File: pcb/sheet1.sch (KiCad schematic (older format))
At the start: 316 parts, among them J16 Aud_Conn, J17 Main_Connector, J18 Cat_Box_Conn, J20 J20, Q1 2N3904, Q3 Q_NPN_BCE, Q4 Q_NPN_BCE, SW1 L_11, SW2 D_10, SW3 E/F_10, Y1 12.096MHz

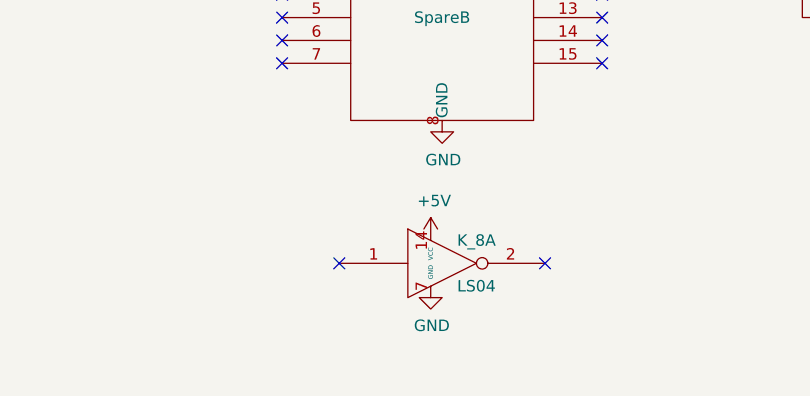
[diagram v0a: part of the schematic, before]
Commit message: Added more power traces
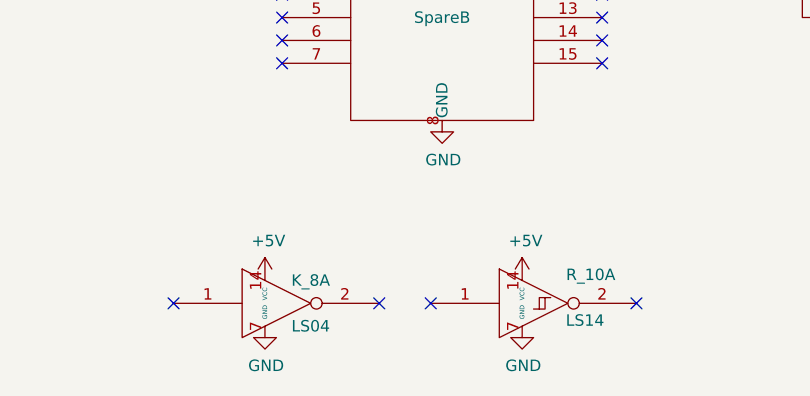
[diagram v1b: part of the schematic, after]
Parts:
- added unit 1 of R_10
- C69, R11: footprint (none) -> Star_Wars_Vector_PCB:GenericComp
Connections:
- net +5V: now also R_10.14 (VCC)
- net GND: now also R_10.7 (GND)
- no-connect marks 180 -> 182
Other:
- moved on the sheet: K_8A
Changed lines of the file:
@@
 F 0 "C69" H 1815 5196 50  0000 L CNN
 F 1 ".1uf" H 1815 5105 50  0000 L CNN
-F 2 "" H 1738 5000 50  0001 C CNN
+F 2 "Star_Wars_Vector_PCB:GenericComp" H 1738 5000 50  0001 C CNN
 F 3 "~" H 1700 5150 50  0001 C CNN
 	1    1700 5150
@@
 F 0 "R11" V 12825 6400 50  0000 C CNN
 F 1 "10k" V 12675 6400 50  0000 C CNN
-F 2 "" V 12790 6390 50  0001 C CNN
+F 2 "Star_Wars_Vector_PCB:GenericComp" V 12790 6390 50  0001 C CNN
 F 3 "~" H 12750 6400 50  0001 C CNN
 	1    12750 6400
@@
 L Asteroids:LS04 K_8
 U 1 1 656FCECD
-P 40425 32050
-F 0 "K_8" H 40575 32150 50  0000 C CNN
-F 1 "LS04" H 40575 31950 50  0000 C CNN
-F 2 "Star_Wars_Vector_PCB:DIP14" H 40425 32050 50  0001 C CNN
-F 3 "" H 40425 32050 50  0001 C CNN
-	1    40425 32050
+P 39700 32225
+F 0 "K_8" H 39850 32325 50  0000 C CNN
+F 1 "LS04" H 39850 32125 50  0000 C CNN
+F 2 "Star_Wars_Vector_PCB:DIP14" H 39700 32225 50  0001 C CNN
+F 3 "" H 39700 32225 50  0001 C CNN
+	1    39700 32225
 	1    0    0    -1
 $EndComp
@@
 L power:GND #PWR0509
 U 1 1 6570845A
-P 40375 32150
-F 0 "#PWR0509" H 40375 31900 50  0001 C CNN
-F 1 "GND" H 40380 31977 50  0000 C CNN
-F 2 "" H 40375 32150 50  0001 C CNN
-F 3 "" H 40375 32150 50  0001 C CNN
-	1    40375 32150
+P 39650 32325
+F 0 "#PWR0509" H 39650 32075 50  0001 C CNN
+F 1 "GND" H 39655 32152 50  0000 C CNN
+F 2 "" H 39650 32325 50  0001 C CNN
+F 3 "" H 39650 32325 50  0001 C CNN
+	1    39650 32325
 	1    0    0    -1
 $EndComp
@@
 L power:+5V #PWR0510
 U 1 1 6570E245
-P 40375 31950
-F 0 "#PWR0510" H 40375 31800 50  0001 C CNN
-F 1 "+5V" H 40390 32123 50  0000 C CNN
-F 2 "" H 40375 31950 50  0001 C CNN
-F 3 "" H 40375 31950 50  0001 C CNN
-	1    40375 31950
+P 39650 32125
+F 0 "#PWR0510" H 39650 31975 50  0001 C CNN
+F 1 "+5V" H 39665 32298 50  0000 C CNN
+F 2 "" H 39650 32125 50  0001 C CNN
+F 3 "" H 39650 32125 50  0001 C CNN
+	1    39650 32125
 	1    0    0    -1
 $EndComp
-NoConn ~ 40875 32050
-NoConn ~ 39975 32050
+NoConn ~ 40150 32225
+NoConn ~ 39250 32225
 NoConn ~ 45200 30250
 NoConn ~ 43950 30350
@@
 	45450 30800 45725 30800
 Connection ~ 45725 30800
+$Comp
+L Star_Wars_Vector_PCB:LS14 R_10
+U 1 1 61140B43
+P 40825 32225
+F 0 "R_10" H 41075 32350 50  0000 C CNN
+F 1 "LS14" H 41050 32150 50  0000 C CNN
+F 2 "" H 40925 32225 50  0001 C CNN
+F 3 "" H 40925 32225 50  0001 C CNN
+	1    40825 32225
+	1    0    0    -1
+$EndComp
+NoConn ~ 41275 32225
+NoConn ~ 40375 32225
+$Comp
+L power:+5V #PWR?
+U 1 1 6193CE8D
+P 40775 32125
+F 0 "#PWR?" H 40775 31975 50  0001 C CNN
+F 1 "+5V" H 40790 32298 50  0000 C CNN
+F 2 "" H 40775 32125 50  0001 C CNN
+F 3 "" H 40775 32125 50  0001 C CNN
+	1    40775 32125
+	1    0    0    -1
+$EndComp
+$Comp
+L power:GND #PWR?
+U 1 1 6194245E
+P 40775 32325
+F 0 "#PWR?" H 40775 32075 50  0001 C CNN
+F 1 "GND" H 40780 32152 50  0000 C CNN
+F 2 "" H 40775 32325 50  0001 C CNN
+F 3 "" H 40775 32325 50  0001 C CNN
+	1    40775 32325
+	1    0    0    -1
+$EndComp
 $EndSCHEMATC

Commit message: Finished the power traces
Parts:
- C81: footprint (none) -> Star_Wars_Vector_PCB:GenericComp
- C93, C94: footprint (none) -> Star_Wars_Main_PCB:Cap1
- R_10: footprint (none) -> Star_Wars_Vector_PCB:DIP14
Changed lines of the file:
@@
 F 0 "C81" H 2665 5921 50  0000 L CNN
 F 1 ".1uf" H 2665 5830 50  0000 L CNN
-F 2 "" H 2588 5725 50  0001 C CNN
+F 2 "Star_Wars_Vector_PCB:GenericComp" H 2588 5725 50  0001 C CNN
 F 3 "~" H 2550 5875 50  0001 C CNN
 	1    2550 5875
@@
 F 0 "C93" H 3640 7996 50  0000 L CNN
 F 1 "10uf 25V" H 3640 7905 50  0000 L CNN
-F 2 "" H 3525 7950 50  0001 C CNN
+F 2 "Star_Wars_Main_PCB:Cap1" H 3525 7950 50  0001 C CNN
 F 3 "~" H 3525 7950 50  0001 C CNN
 	1    3525 7950
@@
 F 0 "C94" H 33090 2046 50  0000 L CNN
 F 1 "4.7uf" H 33090 1955 50  0000 L CNN
-F 2 "" H 32975 2000 50  0001 C CNN
+F 2 "Star_Wars_Main_PCB:Cap1" H 32975 2000 50  0001 C CNN
 F 3 "~" H 32975 2000 50  0001 C CNN
 	1    32975 2000
@@
 F 0 "R_10" H 41075 32350 50  0000 C CNN
 F 1 "LS14" H 41050 32150 50  0000 C CNN
-F 2 "" H 40925 32225 50  0001 C CNN
+F 2 "Star_Wars_Vector_PCB:DIP14" H 40925 32225 50  0001 C CNN
 F 3 "" H 40925 32225 50  0001 C CNN
 	1    40825 32225
@@
 NoConn ~ 40375 32225
 $Comp
-L power:+5V #PWR?
+L power:+5V #PWR0511
 U 1 1 6193CE8D
 P 40775 32125
-F 0 "#PWR?" H 40775 31975 50  0001 C CNN
+F 0 "#PWR0511" H 40775 31975 50  0001 C CNN
 F 1 "+5V" H 40790 32298 50  0000 C CNN
 F 2 "" H 40775 32125 50  0001 C CNN
@@
 $EndComp
 $Comp
-L power:GND #PWR?
+L power:GND #PWR0512
 U 1 1 6194245E
 P 40775 32325
-F 0 "#PWR?" H 40775 32075 50  0001 C CNN
+F 0 "#PWR0512" H 40775 32075 50  0001 C CNN
 F 1 "GND" H 40780 32152 50  0000 C CNN
 F 2 "" H 40775 32325 50  0001 C CNN

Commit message: Added several components
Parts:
- C21, C52, C56, C59, C62, C65, C66, C73, C74, C77, C78, C82, C83, C85, C86, R13, R14, R16, R17, R58: footprint (none) -> Star_Wars_Vector_PCB:GenericComp
- CR2, CR4, CR5, CR6: footprint (none) -> Star_Wars_Vector_PCB:LED
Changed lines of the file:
@@
 F 0 "CR2" V 2264 2758 50  0000 R CNN
 F 1 "BLUE" V 2173 2758 50  0000 R CNN
-F 2 "" H 2225 2875 50  0001 C CNN
+F 2 "Star_Wars_Vector_PCB:LED" H 2225 2875 50  0001 C CNN
 F 3 "~" H 2225 2875 50  0001 C CNN
 	1    2225 2875
@@
 F 0 "C21" H 1390 3746 50  0000 L CNN
 F 1 ".1uf" H 1390 3655 50  0000 L CNN
-F 2 "" H 1313 3550 50  0001 C CNN
+F 2 "Star_Wars_Vector_PCB:GenericComp" H 1313 3550 50  0001 C CNN
 F 3 "~" H 1275 3700 50  0001 C CNN
 	1    1275 3700
@@
 F 0 "C52" H 3090 3746 50  0000 L CNN
 F 1 ".1uf" H 3090 3655 50  0000 L CNN
-F 2 "" H 3013 3550 50  0001 C CNN
+F 2 "Star_Wars_Vector_PCB:GenericComp" H 3013 3550 50  0001 C CNN
 F 3 "~" H 2975 3700 50  0001 C CNN
 	1    2975 3700
@@
 F 0 "C56" H 4790 3746 50  0000 L CNN
 F 1 ".1uf" H 4790 3655 50  0000 L CNN
-F 2 "" H 4713 3550 50  0001 C CNN
+F 2 "Star_Wars_Vector_PCB:GenericComp" H 4713 3550 50  0001 C CNN
 F 3 "~" H 4675 3700 50  0001 C CNN
 	1    4675 3700
@@
 F 0 "C59" H 1815 4471 50  0000 L CNN
 F 1 ".1uf" H 1815 4380 50  0000 L CNN
-F 2 "" H 1738 4275 50  0001 C CNN
+F 2 "Star_Wars_Vector_PCB:GenericComp" H 1738 4275 50  0001 C CNN
 F 3 "~" H 1700 4425 50  0001 C CNN
 	1    1700 4425
@@
 F 0 "C62" H 3090 4471 50  0000 L CNN
 F 1 ".1uf" H 3090 4380 50  0000 L CNN
-F 2 "" H 3013 4275 50  0001 C CNN
+F 2 "Star_Wars_Vector_PCB:GenericComp" H 3013 4275 50  0001 C CNN
 F 3 "~" H 2975 4425 50  0001 C CNN
 	1    2975 4425
@@
 F 0 "C65" H 4365 4471 50  0000 L CNN
 F 1 ".1uf" H 4365 4380 50  0000 L CNN
-F 2 "" H 4288 4275 50  0001 C CNN
+F 2 "Star_Wars_Vector_PCB:GenericComp" H 4288 4275 50  0001 C CNN
 F 3 "~" H 4250 4425 50  0001 C CNN
 	1    4250 4425
@@
 F 0 "C66" H 4790 4471 50  0000 L CNN
 F 1 ".1uf" H 4790 4380 50  0000 L CNN
-F 2 "" H 4713 4275 50  0001 C CNN
+F 2 "Star_Wars_Vector_PCB:GenericComp" H 4713 4275 50  0001 C CNN
 F 3 "~" H 4675 4425 50  0001 C CNN
 	1    4675 4425
@@
 F 0 "C73" H 3515 5196 50  0000 L CNN
 F 1 ".1uf" H 3515 5105 50  0000 L CNN
-F 2 "" H 3438 5000 50  0001 C CNN
+F 2 "Star_Wars_Vector_PCB:GenericComp" H 3438 5000 50  0001 C CNN
 F 3 "~" H 3400 5150 50  0001 C CNN
 	1    3400 5150
@@
 F 0 "C74" H 3940 5196 50  0000 L CNN
 F 1 ".1uf" H 3940 5105 50  0000 L CNN
-F 2 "" H 3863 5000 50  0001 C CNN
+F 2 "Star_Wars_Vector_PCB:GenericComp" H 3863 5000 50  0001 C CNN
 F 3 "~" H 3825 5150 50  0001 C CNN
 	1    3825 5150
@@
 F 0 "C77" H 5215 5196 50  0000 L CNN
 F 1 ".1uf" H 5215 5105 50  0000 L CNN
-F 2 "" H 5138 5000 50  0001 C CNN
+F 2 "Star_Wars_Vector_PCB:GenericComp" H 5138 5000 50  0001 C CNN
 F 3 "~" H 5100 5150 50  0001 C CNN
 	1    5100 5150
@@
 F 0 "C78" H 1390 5921 50  0000 L CNN
 F 1 ".1uf" H 1390 5830 50  0000 L CNN
-F 2 "" H 1313 5725 50  0001 C CNN
+F 2 "Star_Wars_Vector_PCB:GenericComp" H 1313 5725 50  0001 C CNN
 F 3 "~" H 1275 5875 50  0001 C CNN
 	1    1275 5875
@@
 F 0 "C82" H 3090 5921 50  0000 L CNN
 F 1 ".1uf" H 3090 5830 50  0000 L CNN
-F 2 "" H 3013 5725 50  0001 C CNN
+F 2 "Star_Wars_Vector_PCB:GenericComp" H 3013 5725 50  0001 C CNN
 F 3 "~" H 2975 5875 50  0001 C CNN
 	1    2975 5875
@@
 F 0 "C83" H 3515 5921 50  0000 L CNN
 F 1 ".1uf" H 3515 5830 50  0000 L CNN
-F 2 "" H 3438 5725 50  0001 C CNN
+F 2 "Star_Wars_Vector_PCB:GenericComp" H 3438 5725 50  0001 C CNN
 F 3 "~" H 3400 5875 50  0001 C CNN
 	1    3400 5875
@@
 F 0 "C85" H 4365 5921 50  0000 L CNN
 F 1 ".1uf" H 4365 5830 50  0000 L CNN
-F 2 "" H 4288 5725 50  0001 C CNN
+F 2 "Star_Wars_Vector_PCB:GenericComp" H 4288 5725 50  0001 C CNN
 F 3 "~" H 4250 5875 50  0001 C CNN
 	1    4250 5875
@@
 F 0 "C86" H 4790 5921 50  0000 L CNN
 F 1 ".1uf" H 4790 5830 50  0000 L CNN
-F 2 "" H 4713 5725 50  0001 C CNN
+F 2 "Star_Wars_Vector_PCB:GenericComp" H 4713 5725 50  0001 C CNN
 F 3 "~" H 4675 5875 50  0001 C CNN
 	1    4675 5875
@@
 F 0 "R13" V 33925 7425 50  0000 C CNN
 F 1 "1k" V 33925 7600 50  0000 C CNN
-F 2 "" V 34040 7490 50  0001 C CNN
+F 2 "Star_Wars_Vector_PCB:GenericComp" V 34040 7490 50  0001 C CNN
 F 3 "~" H 34000 7500 50  0001 C CNN
 	1    34000 7500
@@
 F 0 "CR4" H 34625 7400 50  0000 C CNN
 F 1 "BLUE LED" H 34600 7175 50  0000 C CNN
-F 2 "" H 34625 7300 50  0001 C CNN
+F 2 "Star_Wars_Vector_PCB:LED" H 34625 7300 50  0001 C CNN
 F 3 "~" H 34625 7300 50  0001 C CNN
 	1    34625 7300
@@
 F 0 "R14" V 33950 7625 50  0000 C CNN
 F 1 "1k" V 33950 7950 50  0000 C CNN
-F 2 "" V 34040 7790 50  0001 C CNN
+F 2 "Star_Wars_Vector_PCB:GenericComp" V 34040 7790 50  0001 C CNN
 F 3 "~" H 34000 7800 50  0001 C CNN
 	1    34000 7800
@@
 F 0 "CR5" H 34475 7850 50  0000 C CNN
 F 1 "BLUE LED" H 34775 7700 50  0000 C CNN
-F 2 "" H 34625 7800 50  0001 C CNN
+F 2 "Star_Wars_Vector_PCB:LED" H 34625 7800 50  0001 C CNN
 F 3 "~" H 34625 7800 50  0001 C CNN
 	1    34625 7800
@@
 F 0 "R58" V 33950 7900 50  0000 C CNN
 F 1 "1k" V 33950 8200 50  0000 C CNN
-F 2 "" V 34065 8065 50  0001 C CNN
+F 2 "Star_Wars_Vector_PCB:GenericComp" V 34065 8065 50  0001 C CNN
 F 3 "~" H 34025 8075 50  0001 C CNN
 	1    34025 8075
@@
 F 0 "CR6" H 34475 8125 50  0000 C CNN
 F 1 "BLUE LED" H 34775 7975 50  0000 C CNN
-F 2 "" H 34625 8075 50  0001 C CNN
+F 2 "Star_Wars_Vector_PCB:LED" H 34625 8075 50  0001 C CNN
 F 3 "~" H 34625 8075 50  0001 C CNN
 	1    34625 8075
@@
 F 0 "R16" V 36450 7450 50  0000 C CNN
 F 1 "1k" V 36450 7700 50  0000 C CNN
-F 2 "" V 36565 7565 50  0001 C CNN
+F 2 "Star_Wars_Vector_PCB:GenericComp" V 36565 7565 50  0001 C CNN
 F 3 "~" H 36525 7575 50  0001 C CNN
 	1    36525 7575
@@
 F 0 "R17" V 36450 7250 50  0000 C CNN
 F 1 "1k" V 36450 7500 50  0000 C CNN
-F 2 "" V 36565 7365 50  0001 C CNN
+F 2 "Star_Wars_Vector_PCB:GenericComp" V 36565 7365 50  0001 C CNN
 F 3 "~" H 36525 7375 50  0001 C CNN
 	1    36525 7375

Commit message: Added more components
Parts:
- C1, C23, C24, C45, C5, C57, C58, C60, C61, C63, C64, C67, C68, C70, C71, C72, C75, C76, C79, C80, C84, C88, C89, C90, C92, R1, R10, R2, R3, R4, R91, R92, R93, R94, R95, R96, R97: footprint (none) -> Star_Wars_Vector_PCB:GenericComp
- C2, C3: footprint (none) -> Star_Wars_Vector_PCB:CapBrown
- J16: footprint (none) -> Star_Wars_Main_PCB:Aud_Con
- L1: footprint (none) -> Star_Wars_Main_PCB:Ind
- Q1: footprint (none) -> Star_Wars_Vector_PCB:GenericTrans
- TP+5V3, TP+5V4, TP3MHZ1, TP6MHZ1, TPCATSTR1, TPDIAGN1, TPE1, TPEVMEM1, TPFIRE/START1, TPGND3, TPGND4, TPHALT1, TPMPAGE1, TPQ1, TPRESET1, TPROM0, TPROM1, TPROM2, TPROM3, TPROM4, TPRW1, TPRWB1, TPWDDIS1: footprint (none) -> Star_Wars_Vector_PCB:TEST_POINT
- Y1: footprint (none) -> Star_Wars_Main_PCB:Y

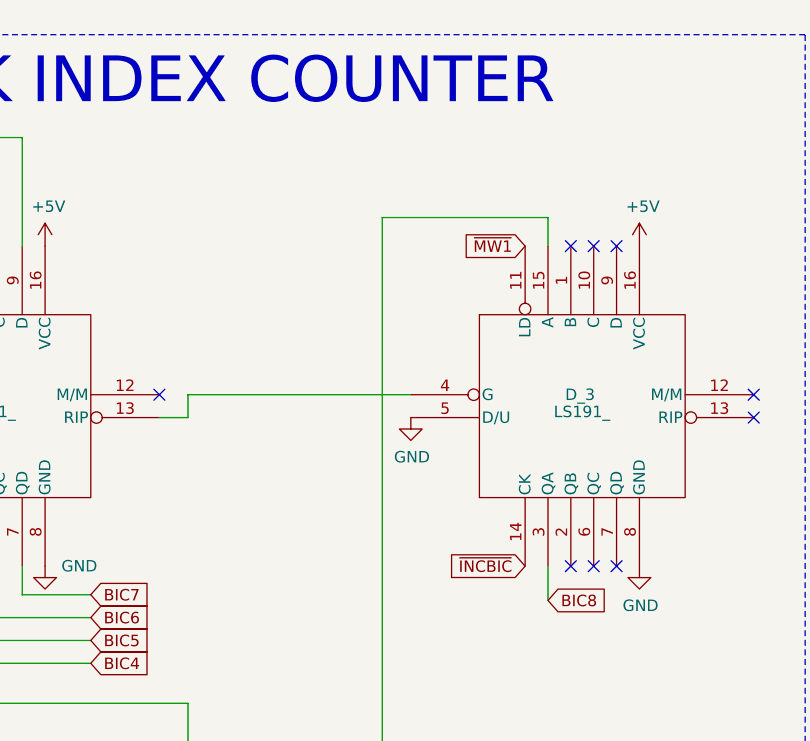
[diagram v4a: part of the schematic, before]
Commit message: 891 unconnected signal remain
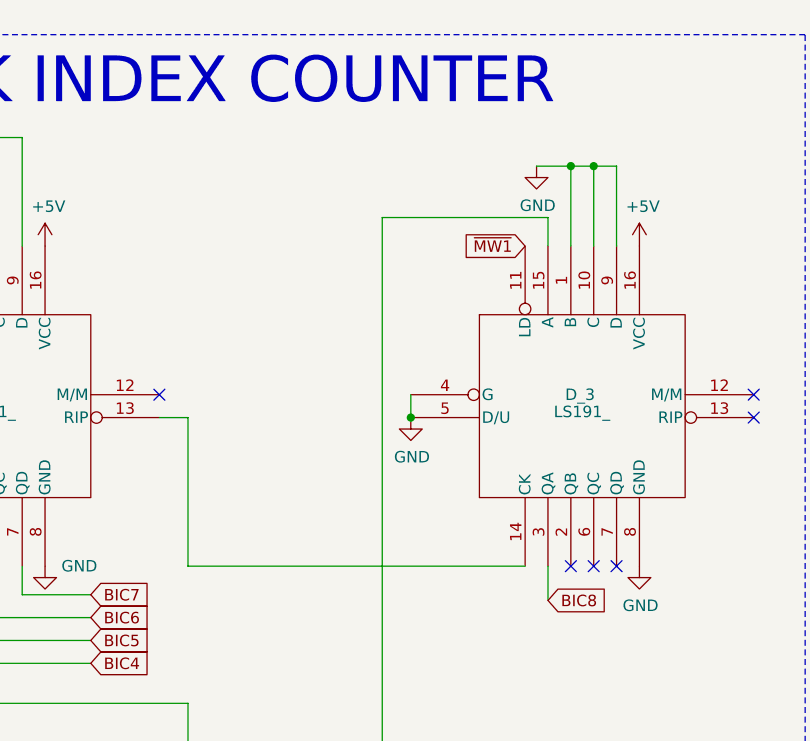
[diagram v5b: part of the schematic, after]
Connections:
- net GND: now also D_3.1 (B), D_3.10 (C), D_3.4 (G), D_3.9 (D)
- net ~INCBIC: no longer D_3.14 (CK)
- net at F_3.13 (RIP): now also D_3.14 (CK); no longer D_3.4 (G)
- no-connect marks 182 -> 179
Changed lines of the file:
@@
 $EndComp
-Wire Wire Line
-	15325 16525 14350 16525
-Wire Wire Line
-	14350 16525 14350 16625
 Wire Wire Line
 	14350 16625 14225 16625
 NoConn ~ 14225 16525
-NoConn ~ 16025 15875
-NoConn ~ 16125 15875
-NoConn ~ 16225 15875
 NoConn ~ 16825 16525
 NoConn ~ 16825 16625
@@
 	1    0    0    -1
 $EndComp
-Text GLabel 15825 15875 0    50   Input ~ 0
-~MW1
-Text GLabel 15825 17275 0    50   Input ~ 0
-~INCBIC
 Text GLabel 15925 17425 2    50   Input ~ 0
 BIC8
@@
 	1    0    0    -1
 $EndComp
+Wire Wire Line
+	15325 16525 15325 16625
+Connection ~ 15325 16625
+Wire Wire Line
+	15825 17275 14350 17275
+Wire Wire Line
+	14350 17275 14350 16625
+Text GLabel 15825 15875 0    50   Input ~ 0
+~MW1
+$Comp
+L power:GND #PWR0513
+U 1 1 65C49D60
+P 15875 15525
+F 0 "#PWR0513" H 15875 15275 50  0001 C CNN
+F 1 "GND" H 15880 15352 50  0000 C CNN
+F 2 "" H 15875 15525 50  0001 C CNN
+F 3 "" H 15875 15525 50  0001 C CNN
+	1    15875 15525
+	1    0    0    -1
+$EndComp
+Wire Wire Line
+	16025 15875 16025 15525
+Wire Wire Line
+	16025 15525 15875 15525
+Wire Wire Line
+	16025 15525 16125 15525
+Wire Wire Line
+	16225 15525 16225 15875
+Connection ~ 16025 15525
+Wire Wire Line
+	16125 15875 16125 15525
+Connection ~ 16125 15525
+Wire Wire Line
+	16125 15525 16225 15525
 $EndSCHEMATC

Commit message: Added more signal traces
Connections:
- net GND: no longer N_11.5 (+), N_11.6 (-)
- net at L/M_9.4 (Q0), L_10.5: no longer R16.1
- net at L/M_9.5 (Q1), L_10.3: no longer R17.1
- net at L_10.4, Q3.1 (B): now also R17.1
- net at L_10.6, Q4.1 (B): now also R16.1
- no-connect marks 179 -> 181
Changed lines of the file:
@@
 $EndComp
 $Comp
-L power:GND #PWR0236
-U 1 1 6B0B3989
-P 6525 5925
-F 0 "#PWR0236" H 6525 5675 50  0001 C CNN
-F 1 "GND" H 6530 5752 50  0000 C CNN
-F 2 "" H 6525 5925 50  0001 C CNN
-F 3 "" H 6525 5925 50  0001 C CNN
-	1    6525 5925
-	1    0    0    -1
-$EndComp
-$Comp
 L power:GND #PWR0237
 U 1 1 6B0B554F
@@
 $EndComp
 Wire Wire Line
-	6600 5925 6525 5925
-Wire Wire Line
-	6600 5725 6525 5725
-Wire Wire Line
-	6525 5725 6525 5925
-Connection ~ 6525 5925
-Wire Wire Line
 	9000 5025 9000 4825
 Wire Wire Line
@@
 	35725 8250 35725 7200
 Wire Wire Line
-	35725 7200 36775 7200
-Wire Wire Line
-	37050 7725 36775 7725
-Wire Wire Line
 	35800 7725 35800 8300
 Wire Wire Line
@@
 	36675 7375 36775 7375
 Wire Wire Line
-	36775 7375 36775 7200
-Connection ~ 36775 7200
-Wire Wire Line
-	36775 7200 37050 7200
-Wire Wire Line
 	36675 7575 36775 7575
-Wire Wire Line
-	36775 7575 36775 7725
-Connection ~ 36775 7725
-Wire Wire Line
-	36775 7725 35800 7725
 $Comp
 L Device:Q_NPN_BCE Q3
@@
 	38400 6950 38400 7000
 Wire Wire Line
-	38100 7200 37950 7200
+	38100 7200 38050 7200
 Wire Wire Line
 	38100 8025 38100 7725
 Wire Wire Line
-	38100 7725 37950 7725
+	38100 7725 38050 7725
 $Comp
 L Switch:SW_DIP_x04 SW1
@@
 Wire Wire Line
 	16125 15525 16225 15525
+NoConn ~ 6600 5725
+NoConn ~ 6600 5925
+Wire Wire Line
+	35800 7725 37050 7725
+Wire Wire Line
+	35725 7200 37050 7200
+Wire Wire Line
+	36775 7375 36775 7450
+Wire Wire Line
+	36775 7450 38050 7450
+Wire Wire Line
+	38050 7450 38050 7200
+Connection ~ 38050 7200
+Wire Wire Line
+	38050 7200 37950 7200
+Wire Wire Line
+	36775 7575 36775 7500
+Wire Wire Line
+	36775 7500 38050 7500
+Wire Wire Line
+	38050 7500 38050 7725
+Connection ~ 38050 7725
+Wire Wire Line
+	38050 7725 37950 7725
 $EndSCHEMATC

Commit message: Added more signal traces
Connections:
- net GND: now also F_3.4 (G)
- net IP7: now also E_6.1; no longer E_6.2
- net S1: now also E_6.2; no longer E_6.1, J16.8 (S1), J20.5 (S1)
- net S2: no longer J16.9 (S2), J20.8 (S2)
- net ~INCBIC: no longer F_3.14 (CK)
- net at E_3.13 (RIP): now also F_3.14 (CK); no longer F_3.4 (G)
- new net S1_: J16.8 (S1), J20.5 (S1)
- new net S2_: J16.9 (S2), J20.8 (S2)
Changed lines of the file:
@@
 $EndComp
 Text GLabel 43850 26150 0    50   Input ~ 0
-S1
+S1_
 Text GLabel 43525 26450 0    50   Input ~ 0
-S2
+S2_
 Text GLabel 43850 26250 0    50   Input ~ 0
 LED1
@@
 $EndComp
 Text GLabel 42175 30825 0    50   Input ~ 0
-S1
+S1_
 Text GLabel 42175 30925 0    50   Input ~ 0
-S2
+S2_
 $Comp
 L Device:CP1 C50
@@
 Wire Wire Line
 	28450 29675 28450 30050
-Wire Wire Line
-	28450 30050 27275 30050
-Wire Wire Line
-	27275 30050 27275 30400
 Text GLabel 28500 30050 2    50   Input ~ 0
 S1
@@
 Text GLabel 27250 29775 0    50   Input ~ 0
 ~ENB
-Text GLabel 27275 30600 0    50   Input ~ 0
+Text GLabel 27275 30400 0    50   Input ~ 0
 IP7
 Text Notes 25300 24975 0    200  ~ 0
@@
 	14350 19500 14350 17875
 Wire Wire Line
-	14350 17875 12575 17875
-Wire Wire Line
-	12575 17875 12575 16525
-Wire Wire Line
-	12575 16525 12725 16525
+	14350 17875 13225 17875
 Text GLabel 13925 17400 2    50   Input ~ 0
 BIC7
@@
 Wire Wire Line
 	13325 17700 13325 17275
-Text GLabel 13000 17500 0    50   Input ~ 0
-~INCBIC
 Wire Wire Line
-	13225 17500 13225 17275
-Wire Wire Line
-	13000 17500 13225 17500
+	13225 17875 13225 17275
 Wire Wire Line
 	12475 15800 12475 18750
@@
 Wire Wire Line
 	38050 7725 37950 7725
+Wire Wire Line
+	12725 16525 12725 16625
+Connection ~ 12725 16625
+Wire Wire Line
+	27275 30600 27050 30600
+Wire Wire Line
+	27050 30600 27050 30050
+Wire Wire Line
+	27050 30050 28450 30050
 $EndSCHEMATC

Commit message: 661 unconnected signal remain
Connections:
- net 1.5GCLK: now also D_9.12 (QC); no longer D_9.13 (QB)
- net 3GCLK: now also D_9.13 (QB); no longer D_9.12 (QC)
- net D0: now also K_9.17 (D0); no longer K_9.21 (D7)
- net D1: now also K_9.14 (D1); no longer K_9.20 (D6)
- net D2: now also K_9.15 (D2); no longer K_9.19 (D5)
- net D3: now also K_9.8 (D3); no longer K_9.18 (D4)
- net D4: now also K_9.18 (D4); no longer K_9.8 (D3)
- net D5: now also K_9.19 (D5); no longer K_9.15 (D2)
- net D6: now also K_9.20 (D6); no longer K_9.14 (D1)
- net D7: now also K_9.21 (D7); no longer K_9.17 (D0)
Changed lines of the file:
@@
 Text GLabel 20000 13100 2    50   Input ~ 0
 D0
-Text GLabel 25625 10050 2    50   Input ~ 0
+Text GLabel 25625 10750 2    50   Input ~ 0
 D7
-Text GLabel 25625 10150 2    50   Input ~ 0
+Text GLabel 25625 10650 2    50   Input ~ 0
 D6
-Text GLabel 25625 10250 2    50   Input ~ 0
+Text GLabel 25625 10550 2    50   Input ~ 0
 D5
-Text GLabel 25625 10350 2    50   Input ~ 0
-D4
 Text GLabel 25625 10450 2    50   Input ~ 0
+D4
+Text GLabel 25625 10350 2    50   Input ~ 0
 D3
-Text GLabel 25625 10550 2    50   Input ~ 0
+Text GLabel 25625 10250 2    50   Input ~ 0
 D2
-Text GLabel 25625 10650 2    50   Input ~ 0
+Text GLabel 25625 10150 2    50   Input ~ 0
 D1
-Text GLabel 25625 10750 2    50   Input ~ 0
+Text GLabel 25625 10050 2    50   Input ~ 0
 D0
 NoConn ~ 25625 11150
@@
 NoConn ~ 5200 16825
 NoConn ~ 5500 16825
-Text GLabel 5050 17175 0    50   Input ~ 0
-1.5GCLK
 Text GLabel 5050 17350 0    50   Input ~ 0
+1.5GCLK
+Text GLabel 5050 17175 0    50   Input ~ 0
 3GCLK
 Wire Wire Line
